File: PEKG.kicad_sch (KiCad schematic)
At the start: 86 parts, among them J1 AudioJack4, J2 AudioJack3_SwitchTR, SW1 SW_DPDT_x2, U12 NCS21802DMR2G, U2 TLV9062, U4 TLV9062, U8 NCS21802DMR2G

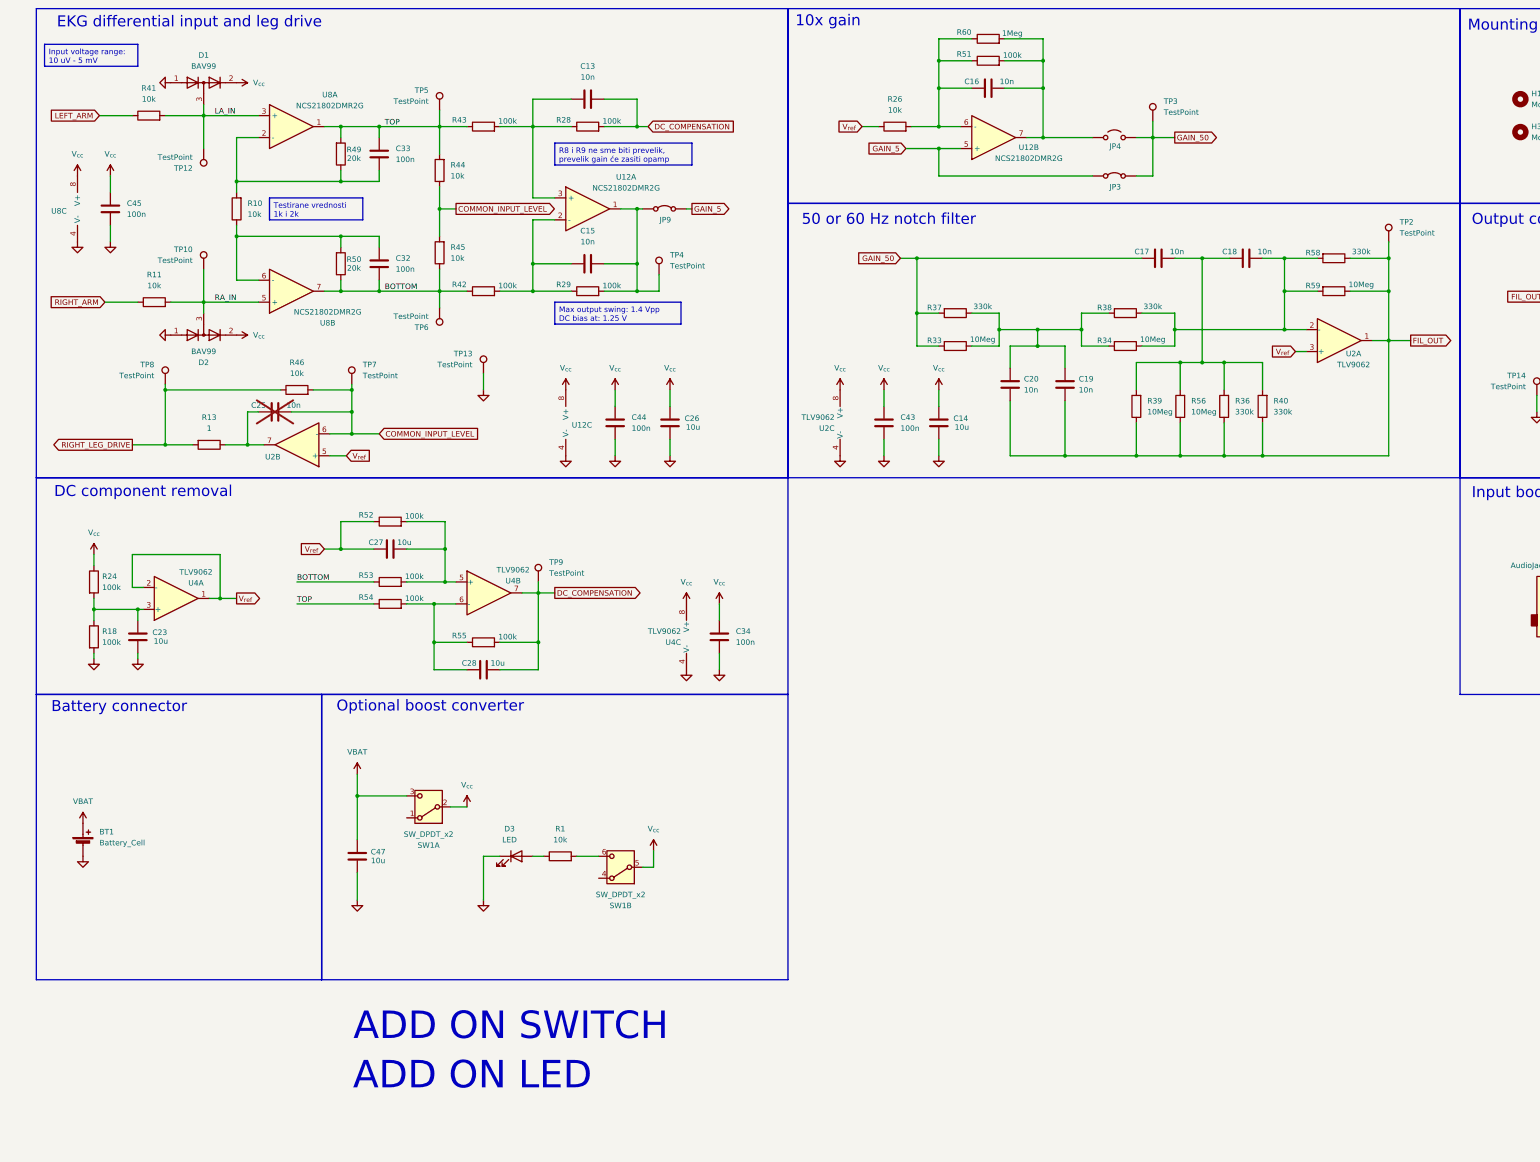
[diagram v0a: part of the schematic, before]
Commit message: added notes, changed opamps
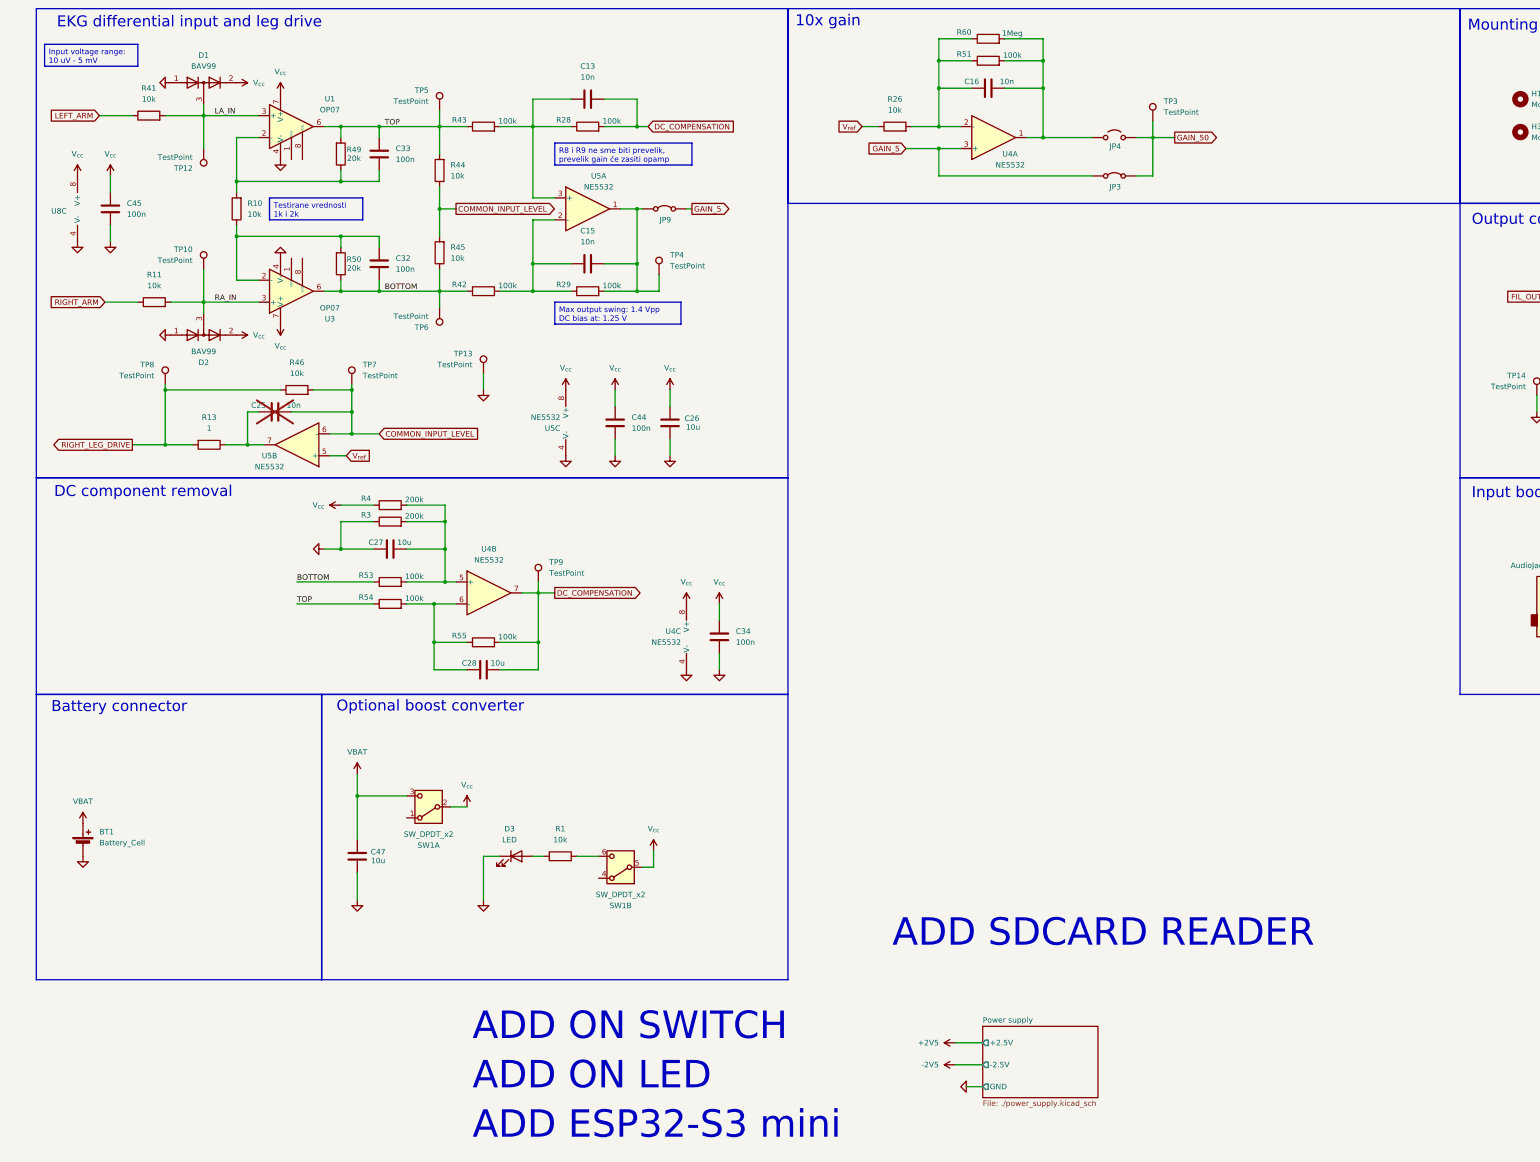
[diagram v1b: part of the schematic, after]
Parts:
- removed C14, C23: 10u, Capacitor_SMD:C_0603_1608Metric_Pad1.08x0.95mm_HandSolder, symbol Device:C
- removed C17, C18, C19, C20: 10n, Capacitor_SMD:C_0603_1608Metric_Pad1.08x0.95mm_HandSolder, symbol Device:C
- removed C43: 100n, Capacitor_SMD:C_0603_1608Metric_Pad1.08x0.95mm_HandSolder, symbol Device:C
- removed R18, R24, R52: 100k, Resistor_SMD:R_0603_1608Metric_Pad0.98x0.95mm_HandSolder, symbol Device:R
- removed R33, R34, R39, R56, R59: 10Meg, Resistor_SMD:R_0603_1608Metric_Pad0.98x0.95mm_HandSolder, symbol Device:R
- removed R36, R37, R38, R40, R58: 330k, Resistor_SMD:R_0603_1608Metric_Pad0.98x0.95mm_HandSolder, symbol Device:R
- removed TP2: TestPoint, TestPoint:TestPoint_Pad_D3.0mm, symbol Connector:TestPoint
- removed U12: NCS21802DMR2G, Package_SO:OnSemi_Micro8, symbol voltmeter_lib:NCS21802DMR2G
- removed U2, U4: TLV9062, Package_SO:SOIC-8_3.9x4.9mm_P1.27mm, symbol Amplifier_Operational:TLV9062
- removed unit 1 of U8
- removed unit 2 of U8
- added R3, R4: 200k, Resistor_SMD:R_0603_1608Metric_Pad0.98x0.95mm_HandSolder, symbol Device:R
- added U1, U3: OP07, Package_SO:SOIC-8_3.9x4.9mm_P1.27mm, symbol Amplifier_Operational:OP07
- added U4: NE5532, symbol Amplifier_Operational:NE5532
- added U5: NE5532, Package_SO:SOIC-8_3.9x4.9mm_P1.27mm, symbol Amplifier_Operational:NE5532
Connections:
- net BOTTOM: now also U3.6
- net COMMON_INPUT_LEVEL: now also U5.6 (-)
- net DC_COMPENSATION: now also U4.7
- net GAIN_5: now also U4.3 (+)
- net GND: now also C27.1, R3.1, U1.4 (V-), U3.4 (V-), U4.4 (V-), U5.4 (V-)
- net LA_IN: now also U1.3 (+)
- net RA_IN: now also U3.3 (+)
- net TOP: now also U1.6
- net V_{cc}: now also R4.1, U1.7 (V+), U3.7 (V+), U4.8 (V+), U5.8 (V+)
- net V_{ref}: now also U5.5 (+); no longer C27.1
- net at C27.2, R53.2: now also R3.2, R4.2, U4.5 (+)
- net at C15.1, JP9.1 (A), R29.2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: now also U5.1
- net at C15.2, R29.1, R42.2: now also U5.2 (-)
- net at C33.1, R10.2, R49.1: now also U1.2 (-)
- net at C16.2, R26.2, R51.1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: now also U4.2 (-)
- net at C16.1, JP4.1 (A), R51.2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: now also U4.1
- net at C13.2, R28.1, R43.2: now also U5.3 (+)
- net at C32.2, R10.1, R50.2: now also U3.2 (-)
- net at C28.1, R54.2, R55.1: now also U4.6 (-)
- net at C25.2, R13.1: now also U5.7
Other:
- added sheet Power supply (./power_supply.kicad_sch)
- note added: "ADD ESP32-S3 mini"
- note added: "ADD SDCARD READER"
- note removed: "50 or 60 Hz notch filter"

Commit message: more readable schematic, bipolar supply
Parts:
- removed C45: 100n, Capacitor_SMD:C_0603_1608Metric_Pad1.08x0.95mm_HandSolder, symbol Device:C
- removed U8: NCS21802DMR2G, Package_SO:OnSemi_Micro8, symbol voltmeter_lib:NCS21802DMR2G
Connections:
- net GND: no longer C26.2, C34.1, C44.1, U1.4 (V-), U3.4 (V-), U4.4 (V-), U5.4 (V-)
- new net V_{ee}: C26.2, C34.1, C44.1, U1.4 (V-), U3.4 (V-), U4.4 (V-), U5.4 (V-)
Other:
- sheet Power supply ports: added V_{cc}, V_{ee}; removed +2.5V, -2.5V
- moved on the sheet: C26, C34, C44, U4C, U5C

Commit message: Added ESP32-S3
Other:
- added sheet MCU (mcu.kicad_sch)
- sheet Power supply ports: added +V_{BAT}, +V_{USB}; removed none
- note removed: "ADD ESP32-S3 mini"
- note removed: "ADD ON LED"
- note removed: "ADD SDCARD READER"
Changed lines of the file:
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@@
 		)
 	)
-	(text "ADD SDCARD READER\n"
-		(exclude_from_sim no)
-		(at 255.27 143.51 0)
-		(effects
-			(font
-				(size 6.35 6.35)
-			)
-		)
-	)
 	(text "10x gain"
 		(exclude_from_sim no)
@@
 		)
 	)
-	(text "ADD ON LED\n"
-		(exclude_from_sim no)
-		(at 204.47 118.11 0)
-		(effects
-			(font
-				(size 6.35 6.35)
-			)
-			(justify left)
-		)
-	)
 	(text "Optional boost converter"
 		(exclude_from_sim no)
@@
 		)
 	)
-	(text "ADD ESP32-S3 mini"
-		(exclude_from_sim no)
-		(at 204.47 129.54 0)
-		(effects
-			(font
-				(size 6.35 6.35)
-			)
-			(justify left)
-		)
-	)
 	(text "DC component removal"
 		(exclude_from_sim no)
@@
 	(wire
 		(pts
+			(xy 245.11 198.12) (xy 252.73 198.12)
+		)
+		(stroke
+			(width 0)
+			(type default)
+		)
+	)
+	(wire
+		(pts
 			(xy 86.36 189.23) (xy 86.36 194.31)
 		)
@@
 	(wire
 		(pts
-			(xy 220.98 76.2) (xy 224.79 76.2)
+			(xy 267.97 204.47) (xy 271.78 204.47)
 		)
 		(stroke
@@
 	(wire
 		(pts
-			(xy 224.79 81.28) (xy 220.98 81.28)
+			(xy 271.78 209.55) (xy 267.97 209.55)
 		)
 		(stroke
@@
 	(wire
 		(pts
-			(xy 224.79 71.12) (xy 220.98 71.12)
+			(xy 271.78 199.39) (xy 267.97 199.39)
 		)
 		(stroke
@@
 	(wire
 		(pts
+			(xy 245.11 201.93) (xy 252.73 201.93)
+		)
+		(stroke
+			(width 0)
+			(type default)
+		)
+	)
+	(wire
+		(pts
 			(xy 270.51 38.1) (xy 270.51 41.91)
 		)
@@
 	(symbol
 		(lib_id "Simulation_SPICE:0")
-		(at 224.79 76.2 90)
+		(at 271.78 204.47 90)
 		(unit 1)
 		(exclude_from_sim no)
@@
 		(fields_autoplaced yes)
 		(property "Reference" "#GND01"
-			(at 227.33 76.2 0)
+			(at 274.32 204.47 0)
 			(effects
 				(font
@@
 		)
 		(property "Value" "0"
-			(at 222.25 76.2 0)
+			(at 269.24 204.47 0)
 			(effects
 				(font
@@
 		)
 		(property "Footprint" ""
-			(at 224.79 76.2 0)
+			(at 271.78 204.47 0)
 			(effects
 				(font
@@
 		)
 		(property "Datasheet" "~"
-			(at 224.79 76.2 0)
+			(at 271.78 204.47 0)
 			(effects
 				(font
@@
 		)
 		(property "Description" ""
-			(at 224.79 76.2 0)
+			(at 271.78 204.47 0)
 			(effects
 				(font
@@
 	(symbol
 		(lib_id "power:VCC")
-		(at 224.79 81.28 270)
+		(at 271.78 209.55 270)
 		(unit 1)
 		(exclude_from_sim no)
@@
 		(fields_autoplaced yes)
 		(property "Reference" "#PWR010"
-			(at 220.98 81.28 0)
+			(at 267.97 209.55 0)
 			(effects
 				(font
@@
 		)
 		(property "Value" "V_{ee}"
-			(at 228.6 81.2799 90)
+			(at 275.59 209.5499 90)
 			(effects
 				(font
@@
 		)
 		(property "Footprint" ""
-			(at 224.79 81.28 0)
+			(at 271.78 209.55 0)
 			(effects
 				(font
@@
 		)
 		(property "Datasheet" ""
-			(at 224.79 81.28 0)
+			(at 271.78 209.55 0)
 			(effects
 				(font
@@
 		)
 		(property "Description" "Power symbol creates a global label with name \"VCC\""
-			(at 224.79 81.28 0)
+			(at 271.78 209.55 0)
 			(effects
 				(font
@@
 	(symbol
 		(lib_id "power:VCC")
-		(at 224.79 71.12 270)
+		(at 271.78 199.39 270)
 		(unit 1)
 		(exclude_from_sim no)
@@
 		(fields_autoplaced yes)
 		(property "Reference" "#PWR09"
-			(at 220.98 71.12 0)
+			(at 267.97 199.39 0)
 			(effects
 				(font
@@
 		)
 		(property "Value" "V_{cc}"
-			(at 228.6 71.1199 90)
+			(at 275.59 199.3899 90)
 			(effects
 				(font
@@
 		)
 		(property "Footprint" ""
-			(at 224.79 71.12 0)
+			(at 271.78 199.39 0)
 			(effects
 				(font
@@
 		)
 		(property "Datasheet" ""
-			(at 224.79 71.12 0)
+			(at 271.78 199.39 0)
 			(effects
 				(font
@@
 		)
 		(property "Description" "Power symbol creates a global label with name \"VCC\""
-			(at 224.79 71.12 0)
+			(at 271.78 199.39 0)
 			(effects
 				(font
@@
 	)
 	(sheet
-		(at 205.74 68.58)
+		(at 229.87 196.85)
+		(size 15.24 15.24)
+		(exclude_from_sim no)
+		(in_bom yes)
+		(on_board yes)
+		(dnp no)
+		(fields_autoplaced yes)
+		(stroke
+			(width 0.1524)
+			(type solid)
+		)
+		(fill
+			(color 0 0 0 0.0000)
+		)
+		(property "Sheetname" "MCU"
+			(at 229.87 196.1384 0)
+			(effects
+				(font
+					(size 1.27 1.27)
+				)
+				(justify left bottom)
+			)
+		)
+		(property "Sheetfile" "mcu.kicad_sch"
+			(at 229.87 212.6746 0)
+			(effects
+				(font
+					(size 1.27 1.27)
+				)
+				(justify left top)
+			)
+		)
+		(pin "+V_{BAT}" input
+			(at 245.11 201.93 0)
+			(effects
+				(font
+					(size 1.27 1.27)
+				)
+				(justify right)
+			)
+		)
+		(pin "+V_{USB}" output
+			(at 245.11 198.12 0)
+			(effects
+				(font
+					(size 1.27 1.27)
+				)
+				(justify right)
+			)
+		)
+		(instances
+			(project "PEKG"
+				(path "/6b6ace37-3aeb-4177-8f53-de4683f890d9"
+					(page "3")
+				)
+			)
+		)
+	)
+	(sheet
+		(at 252.73 196.85)
 		(size 15.24 15.24)
 		(exclude_from_sim no)
@@
 		)
 		(property "Sheetname" "Power supply"
-			(at 205.74 67.8684 0)
+			(at 252.73 196.1384 0)
 			(effects
 				(font
@@
 		)
 		(property "Sheetfile" "./power_supply.kicad_sch"
-			(at 205.74 84.4046 0)
+			(at 252.73 212.6746 0)
 			(effects
 				(font
@@
 		)
 		(pin "V_{ee}" output
-			(at 220.98 81.28 0)
+			(at 267.97 209.55 0)
 			(effects
 				(font
@@
 		)
 		(pin "V_{cc}" output
-			(at 220.98 71.12 0)
+			(at 267.97 199.39 0)
 			(effects
 				(font
@@
 		)
 		(pin "GND" output
-			(at 220.98 76.2 0)
+			(at 267.97 204.47 0)
 			(effects
 				(font
@@
 			)
 		)
+		(pin "+V_{BAT}" output
+			(at 252.73 201.93 180)
+			(effects
+				(font
+					(size 1.27 1.27)
+				)
+				(justify left)
+			)
+		)
+		(pin "+V_{USB}" input
+			(at 252.73 198.12 180)
+			(effects
+				(font
+					(size 1.27 1.27)
+				)
+				(justify left)
+			)
+		)

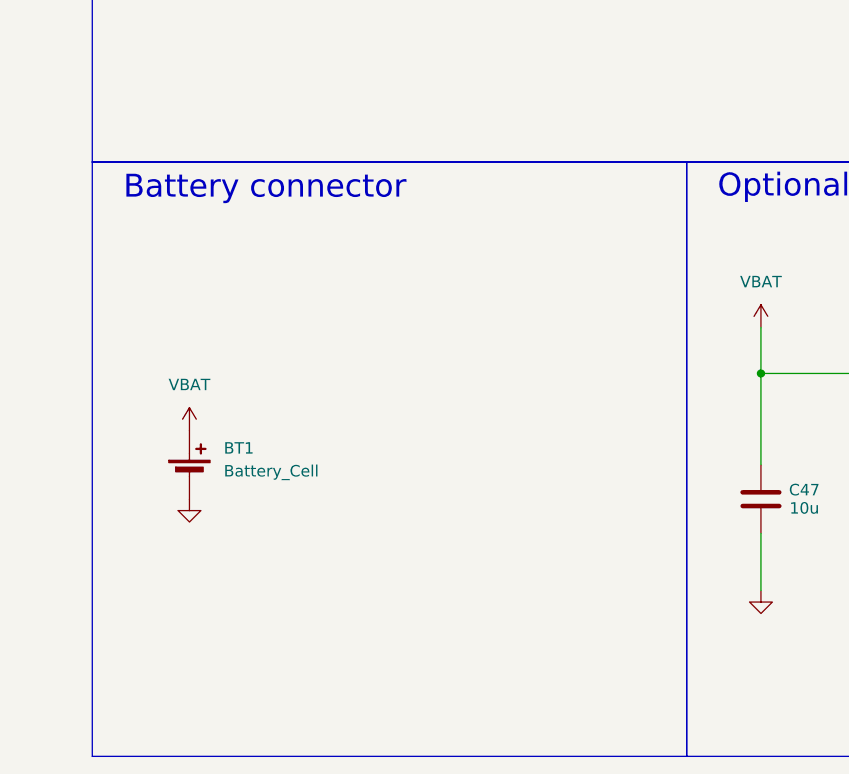
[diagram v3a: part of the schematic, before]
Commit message: connected SD and ESP
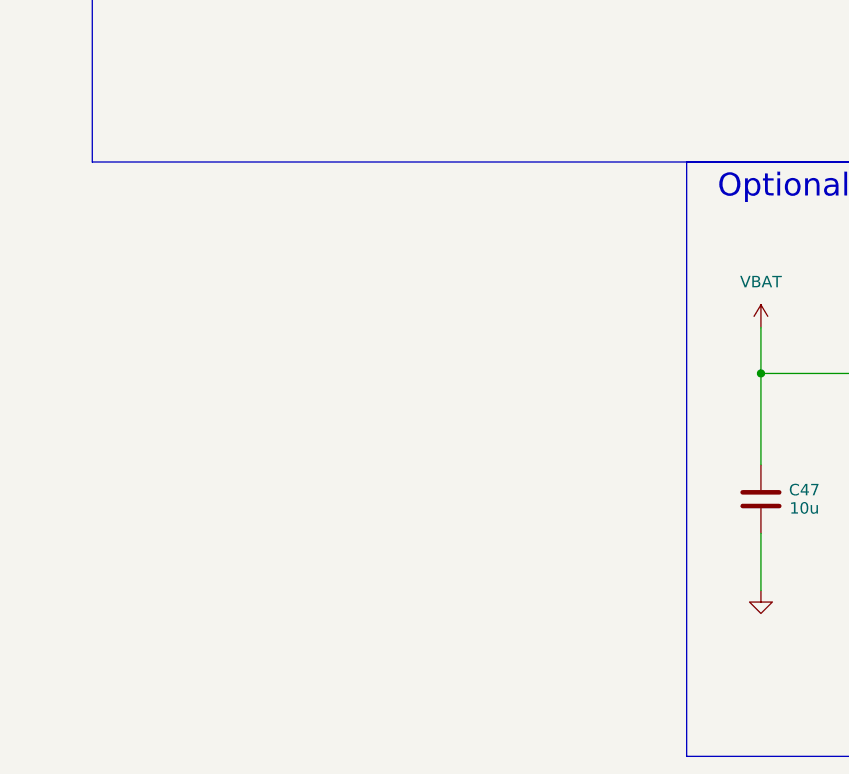
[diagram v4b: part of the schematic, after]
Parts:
- removed BT1: Battery_Cell, PEKG:MG_battery_holder, symbol Device:Battery_Cell
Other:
- note removed: "Battery connector"
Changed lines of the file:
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@@
 	)
 	(rectangle
-		(start 12.065 170.815)
-		(end 78.105 236.855)
-		(stroke
-			(width 0)
-			(type default)
-		)
-		(fill
-			(type none)
-		)
-	)
-	(rectangle
 		(start 341.63 57.15)
 		(end 407.67 120.65)
@@
 		)
 	)
-	(text "Battery connector\n"
-		(exclude_from_sim no)
-		(at 31.242 173.736 0)
-		(effects
-			(font
-				(size 2.54 2.54)
-			)
-		)
-	)
 	(text "EKG differential input and leg drive"
 		(exclude_from_sim no)
@@
 	)
 	(symbol
-		(lib_id "power:VCC")
-		(at 22.86 200.66 0)
-		(unit 1)
-		(exclude_from_sim no)
-		(in_bom yes)
-		(on_board yes)
-		(dnp no)
-		(fields_autoplaced yes)
-		(property "Reference" "#PWR092"
-			(at 22.86 204.47 0)
-			(effects
-				(font
-					(size 1.27 1.27)
-				)
-				(hide yes)
-			)
-		)
-		(property "Value" "VBAT"
-			(at 22.86 195.58 0)
-			(effects
-				(font
-					(size 1.27 1.27)
-				)
-			)
-		)
-		(property "Footprint" ""
-			(at 22.86 200.66 0)
-			(effects
-				(font
-					(size 1.27 1.27)
-				)
-				(hide yes)
-			)
-		)
-		(property "Datasheet" ""
-			(at 22.86 200.66 0)
-			(effects
-				(font
-					(size 1.27 1.27)
-				)
-				(hide yes)
-			)
-		)
-		(property "Description" "Power symbol creates a global label with name \"VCC\""
-			(at 22.86 200.66 0)
-			(effects
-				(font
-					(size 1.27 1.27)
-				)
-				(hide yes)
-			)
-		)
-		(pin "1"
-		)
-		(instances
-			(project "PEKG"
-				(path "/6b6ace37-3aeb-4177-8f53-de4683f890d9"
-					(reference "#PWR092")
-					(unit 1)
-				)
-			)
-		)
-	)
-	(symbol
 		(lib_id "Device:C")
 		(at 139.7 71.12 270)
@@
 	)
 	(symbol
-		(lib_id "Device:Battery_Cell")
-		(at 22.86 205.74 0)
-		(unit 1)
-		(exclude_from_sim no)
-		(in_bom yes)
-		(on_board yes)
-		(dnp no)
-		(fields_autoplaced yes)
-		(property "Reference" "BT1"
-			(at 26.67 202.6284 0)
-			(effects
-				(font
-					(size 1.27 1.27)
-				)
-				(justify left)
-			)
-		)
-		(property "Value" "Battery_Cell"
-			(at 26.67 205.1684 0)
-			(effects
-				(font
-					(size 1.27 1.27)
-				)
-				(justify left)
-			)
-		)
-		(property "Footprint" "PEKG:MG_battery_holder"
-			(at 22.86 204.216 90)
-			(effects
-				(font
-					(size 1.27 1.27)
-				)
-				(hide yes)
-			)
-		)
-		(property "Datasheet" "~"
-			(at 22.86 204.216 90)
-			(effects
-				(font
-					(size 1.27 1.27)
-				)
-				(hide yes)
-			)
-		)
-		(property "Description" "Single-cell battery"
-			(at 22.86 205.74 0)
-			(effects
-				(font
-					(size 1.27 1.27)
-				)
-				(hide yes)
-			)
-		)
-		(pin "1"
-		)
-		(pin "2"
-		)
-		(instances
-			(project ""
-				(path "/6b6ace37-3aeb-4177-8f53-de4683f890d9"
-					(reference "BT1")
-					(unit 1)
-				)
-			)
-		)
-	)
-	(symbol
 		(lib_id "Device:R")
 		(at 210.82 39.37 90)
@@
 					(unit 1)
 				)
-			)
-		)
-	)
-	(symbol
-		(lib_id "power:GND")
-		(at 22.86 208.28 0)
-		(unit 1)
-		(exclude_from_sim no)
-		(in_bom yes)
-		(on_board yes)
-		(dnp no)
-		(fields_autoplaced yes)
-		(property "Reference" "#PWR0102"
-			(at 22.86 214.63 0)
-			(effects
-				(font
-					(size 1.27 1.27)
-				)
-				(hide yes)
-			)
-		)
-		(property "Value" "GND"
-			(at 22.86 213.36 0)
-			(effects
-				(font
-					(size 1.27 1.27)
-				)
-				(hide yes)
-			)
-		)
-		(property "Footprint" ""
-			(at 22.86 208.28 0)
-			(effects
-				(font
-					(size 1.27 1.27)
-				)
-				(hide yes)
-			)
-		)
-		(property "Datasheet" ""
-			(at 22.86 208.28 0)
-			(effects
-				(font
-					(size 1.27 1.27)
-				)
-				(hide yes)
-			)
-		)
-		(property "Description" "Power symbol creates a global label with name \"GND\" , ground"
-			(at 22.86 208.28 0)
-			(effects
-				(font
-					(size 1.27 1.27)
-				)
-				(hide yes)
-			)
-		)
-		(pin "1"
-		)
-		(instances
-			(project "PEKG"
-				(path "/6b6ace37-3aeb-4177-8f53-de4683f890d9"
-					(reference "#PWR0102")
-					(unit 1)
-				)
